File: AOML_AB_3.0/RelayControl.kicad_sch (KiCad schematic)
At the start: 45 parts, among them IC1 CD4043BDR, IC2 CD4043BDR, J5 Conn_01x03, K1 TX2-L2-5V, K10 TX2-L2-5V, K11 TX2-L2-5V, K13 TX2-L2-5V, K2 TX2-L2-5V, K3 TX2-L2-5V, K4 TX2-L2-5V, K5 TX2-L2-5V, K6 TX2-L2-5V, K7 TX2-L2-5V, K8 TX2-L2-5V, K9 TX2-L2-5V, U10 TLP170AM, U11 TLP170AM, U12 TLP170AM, U13 TLP170AM, U14 TLP170AM, U15 TLP170AM, U16 TLP170AM, U17 TLP170AM, U5 ULN2003ADR

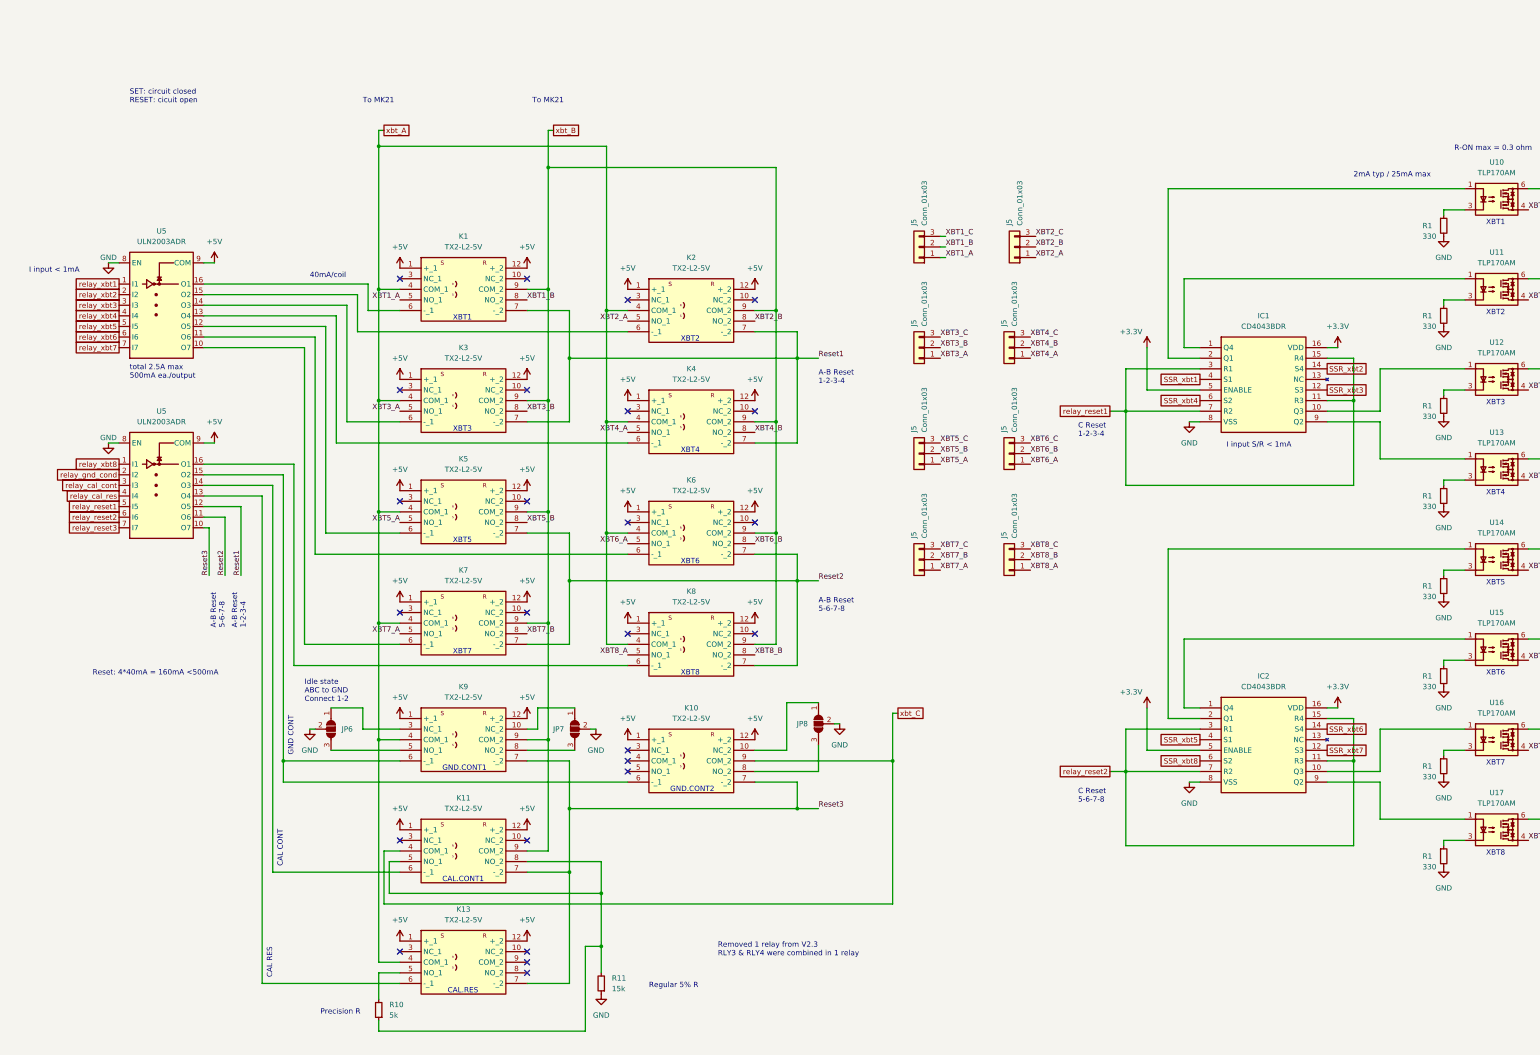
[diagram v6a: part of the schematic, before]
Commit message: Microcontroller pin connections reorganized, test back ground plane routed
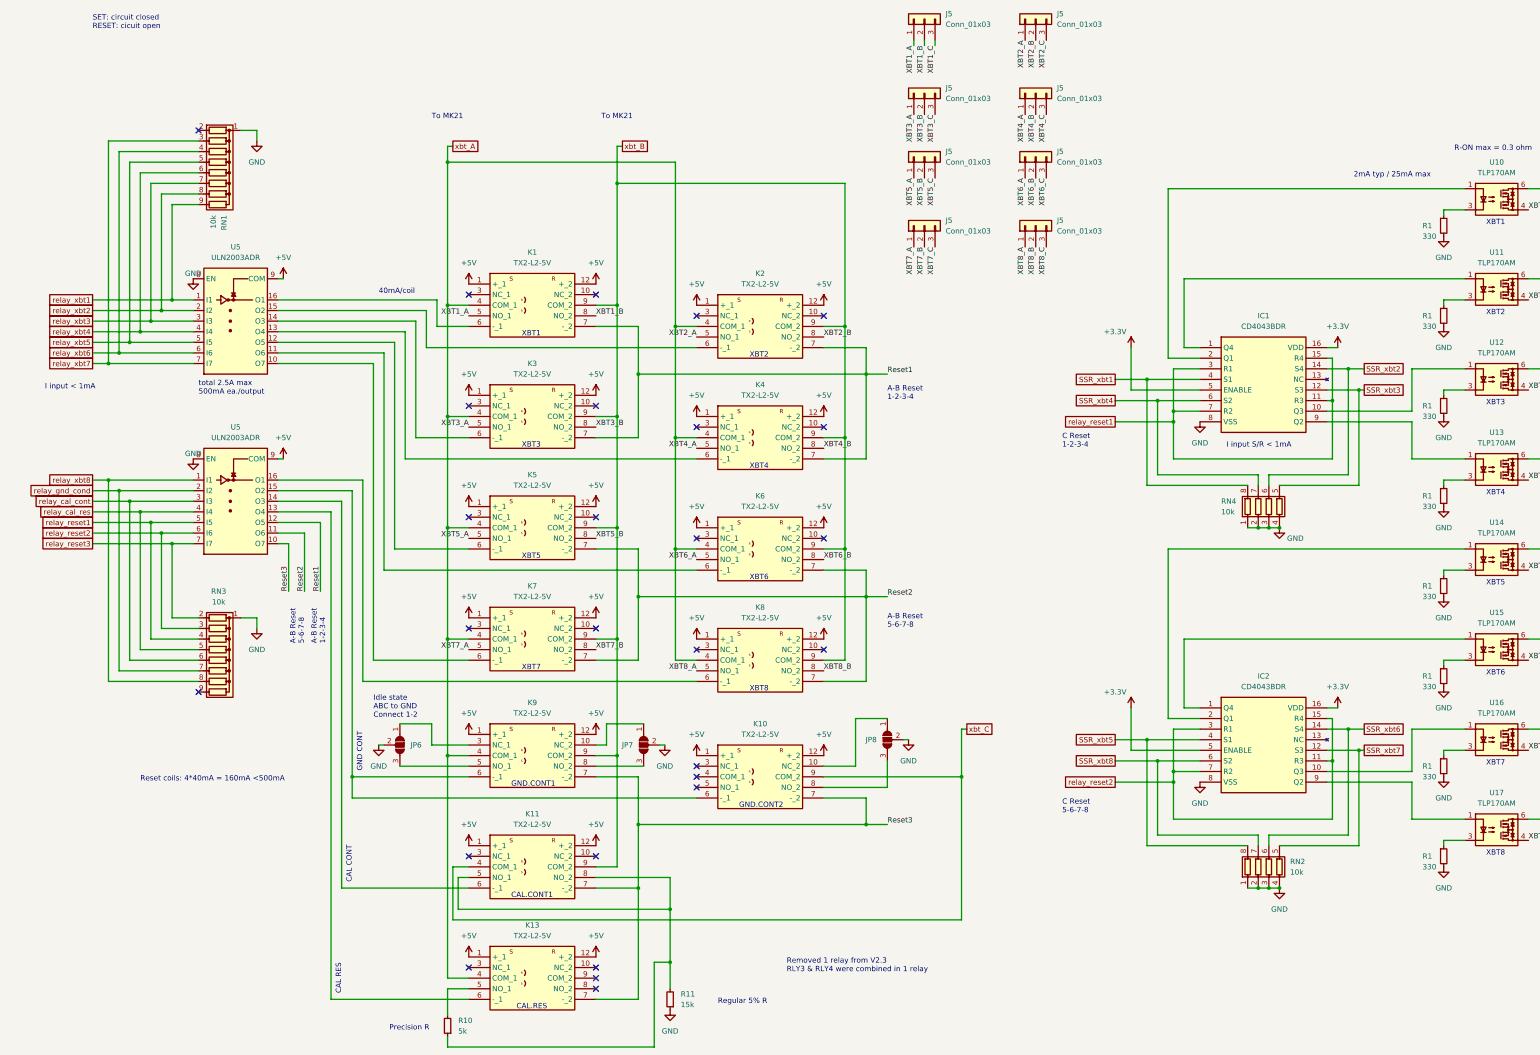
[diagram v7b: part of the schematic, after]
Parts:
- added RN1, RN3: 10k, Resistor_network-10k:SMT_JR-0710KL_YAG, symbol Device:R_Network08
- added RN2, RN4: 10k, Resistor_network_x4_10k-1204:RESCAXS80P320X160X70-8N, symbol Device:R_Pack04
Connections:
- net GND: now also RN1.1 (common), RN2.1 (R1.1), RN2.2 (R2.1), RN2.3 (R3.1), RN2.4 (R4.1), RN3.1 (common), RN4.1 (R1.1), RN4.2 (R2.1), RN4.3 (R3.1), RN4.4 (R4.1)
- net SSR_xbt1: now also RN4.8 (R1.2)
- net SSR_xbt2: now also RN4.6 (R3.2)
- net SSR_xbt3: now also RN4.5 (R4.2)
- net SSR_xbt4: now also RN4.7 (R2.2)
- net SSR_xbt5: now also RN2.8 (R1.2)
- net SSR_xbt6: now also RN2.6 (R3.2)
- net SSR_xbt7: now also RN2.5 (R4.2)
- net SSR_xbt8: now also RN2.7 (R2.2)
- net relay_cal_cont: now also RN3.6 (R5)
- net relay_cal_res: now also RN3.5 (R4)
- net relay_gnd_cond: now also RN3.7 (R6)
- net relay_reset1: now also RN3.4 (R3)
- net relay_reset2: now also RN3.3 (R2)
- net relay_reset3: now also RN3.2 (R1)
- net relay_xbt1: now also RN1.9 (R8)
- net relay_xbt2: now also RN1.8 (R7)
- net relay_xbt3: now also RN1.7 (R6)
- net relay_xbt4: now also RN1.6 (R5)
- net relay_xbt5: now also RN1.5 (R4)
- net relay_xbt6: now also RN1.4 (R3)
- net relay_xbt7: now also RN1.3 (R2)
- net relay_xbt8: now also RN3.8 (R7)
- no-connect marks 25 -> 27
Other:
- note added: "Reset coils: 4*40mA = 160mA <500mA"
- note removed: "Reset: 4*40mA = 160mA <500mA"
- moved on the sheet: J5, JP6, JP7, JP8, K1, K10, K11, K13, K2, K3, K4, K5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

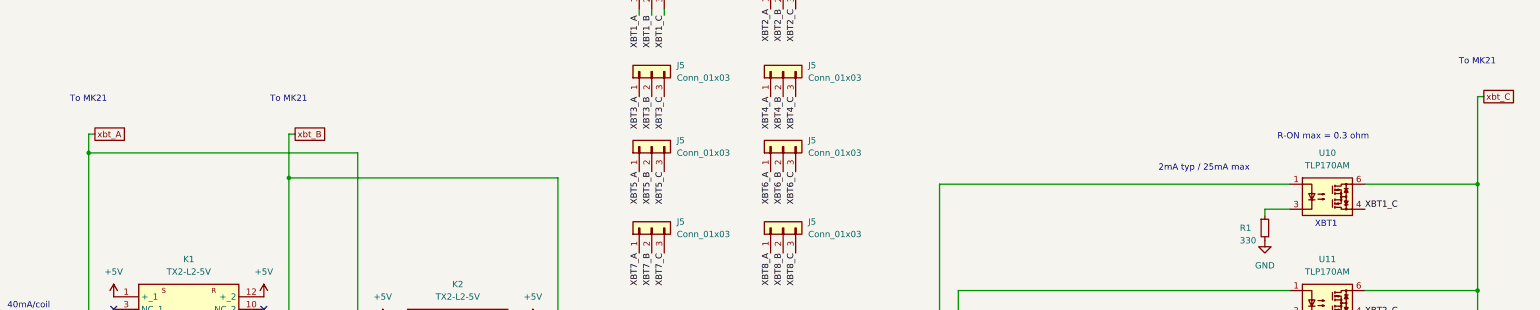
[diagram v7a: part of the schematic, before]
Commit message: test pads added, no tracks yet
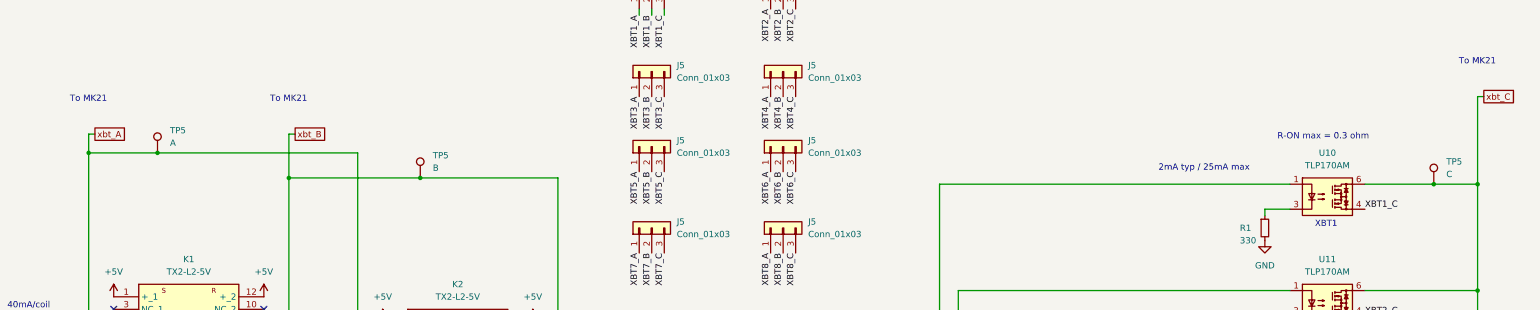
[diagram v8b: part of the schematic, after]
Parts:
- added TP5: B, TestPoint:TestPoint_Pad_1.0x1.0mm, symbol Connector:TestPoint
- added TP5: C, TestPoint:TestPoint_Pad_1.0x1.0mm, symbol Connector:TestPoint
- added TP5: A, TestPoint:TestPoint_Pad_1.0x1.0mm, symbol Connector:TestPoint
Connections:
- net xbt_A: now also TP5.1
- net xbt_B: now also TP5.1
- net xbt_C: now also TP5.1
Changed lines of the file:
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@@
   (junction (at 43.18 91.44) (diameter 0) (color 0 0 0 0)
   )
+  (junction (at 181.61 58.42) (diameter 0) (color 0 0 0 0)
+  )
   (junction (at 33.02 129.54) (diameter 0) (color 0 0 0 0)
   )
@@
   (junction (at 154.94 195.58) (diameter 0) (color 0 0 0 0)
   )
+  (junction (at 387.35 59.69) (diameter 0) (color 0 0 0 0)
+  )
   (junction (at 114.3 53.34) (diameter 0) (color 0 0 0 0)
   )
@@
   (junction (at 114.3 114.3) (diameter 0) (color 0 0 0 0)
   )
+  (junction (at 128.27 53.34) (diameter 0) (color 0 0 0 0)
+  )
   (junction (at 396.24 167.64) (diameter 0) (color 0 0 0 0)
   )
@@
     (stroke (width 0) (type default))
   )
+  (wire (pts (xy 181.61 58.42) (xy 154.94 58.42))
+    (stroke (width 0) (type default))
+  )
   (wire (pts (xy 160.02 119.38) (xy 160.02 104.14))
     (stroke (width 0) (type default))
@@
     (stroke (width 0) (type default))
   )
-  (wire (pts (xy 209.55 58.42) (xy 154.94 58.42))
+  (wire (pts (xy 209.55 58.42) (xy 181.61 58.42))
     (stroke (width 0) (type default))
   )
@@
     (stroke (width 0) (type default))
   )
-  (wire (pts (xy 114.3 53.34) (xy 168.91 53.34))
+  (wire (pts (xy 114.3 53.34) (xy 128.27 53.34))
     (stroke (width 0) (type default))
   )
@@
     (stroke (width 0) (type default))
   )
+  (wire (pts (xy 128.27 53.34) (xy 168.91 53.34))
+    (stroke (width 0) (type default))
+  )
   (wire (pts (xy 353.06 172.72) (xy 358.14 172.72))
     (stroke (width 0) (type default))
@@
     (stroke (width 0) (type default))
   )
+  (wire (pts (xy 387.35 59.69) (xy 396.24 59.69))
+    (stroke (width 0) (type default))
+  )
   (wire (pts (xy 73.66 99.06) (xy 99.06 99.06))
     (stroke (width 0) (type default))
@@
     (stroke (width 0) (type default))
   )
-  (wire (pts (xy 373.38 59.69) (xy 396.24 59.69))
+  (wire (pts (xy 373.38 59.69) (xy 387.35 59.69))
     (stroke (width 0) (type default))
   )
@@
     )
   )
+  (symbol (lib_id "Connector:TestPoint") (at 181.61 58.42 0) (unit 1)
+    (in_bom yes) (on_board yes) (dnp no) (fields_autoplaced)
+    (property "Reference" "TP5" (at 184.15 53.848 0)
+      (effects (font (size 1.27 1.27)) (justify left))
+    )
+    (property "Value" "B" (at 184.15 56.388 0)
+      (effects (font (size 1.27 1.27)) (justify left))
+    )
+    (property "Footprint" "TestPoint:TestPoint_Pad_1.0x1.0mm" (at 186.69 58.42 0)
+      (effects (font (size 1.27 1.27)) hide)
+    )
+    (property "Datasheet" "~" (at 186.69 58.42 0)
+      (effects (font (size 1.27 1.27)) hide)
+    )
+    (pin "1")
+    (instances
+      (project "AOML_AB_3.0"
+        (path "/6a222f58-627e-41ff-951d-9ad8d2e0d7a2"
+          (reference "TP5") (unit 1)
+        )
+        (path "/6a222f58-627e-41ff-951d-9ad8d2e0d7a2/69365a30-fc6f-418a-bc31-d76af2fc83f6"
+          (reference "TP11") (unit 1)
+        )
+      )
+    )
+  )
   (symbol (lib_id "Device:R_Pack04") (at 311.15 222.25 0) (unit 1)
     (in_bom yes) (on_board yes) (dnp no) (fields_autoplaced)
@@
     )
   )
+  (symbol (lib_id "Connector:TestPoint") (at 387.35 59.69 0) (unit 1)
+    (in_bom yes) (on_board yes) (dnp no) (fields_autoplaced)
+    (property "Reference" "TP5" (at 389.89 55.118 0)
+      (effects (font (size 1.27 1.27)) (justify left))
+    )
+    (property "Value" "C" (at 389.89 57.658 0)
+      (effects (font (size 1.27 1.27)) (justify left))
+    )
+    (property "Footprint" "TestPoint:TestPoint_Pad_1.0x1.0mm" (at 392.43 59.69 0)
+      (effects (font (size 1.27 1.27)) hide)
+    )
+    (property "Datasheet" "~" (at 392.43 59.69 0)
+      (effects (font (size 1.27 1.27)) hide)
+    )
+    (pin "1")
+    (instances
+      (project "AOML_AB_3.0"
+        (path "/6a222f58-627e-41ff-951d-9ad8d2e0d7a2"
+          (reference "TP5") (unit 1)
+        )
+        (path "/6a222f58-627e-41ff-951d-9ad8d2e0d7a2/69365a30-fc6f-418a-bc31-d76af2fc83f6"
+          (reference "TP12") (unit 1)
+        )
+      )
+    )
+  )
   (symbol (lib_id "power:+5V") (at 119.38 135.89 0) (unit 1)
     (in_bom yes) (on_board yes) (dnp no) (fields_autoplaced)
@@
         )
       )
+    )
+  )
+  (symbol (lib_id "Connector:TestPoint") (at 128.27 53.34 0) (unit 1)
+    (in_bom yes) (on_board yes) (dnp no) (fields_autoplaced)
+    (property "Reference" "TP5" (at 130.81 48.768 0)
+      (effects (font (size 1.27 1.27)) (justify left))
+    )
+    (property "Value" "A" (at 130.81 51.308 0)
+      (effects (font (size 1.27 1.27)) (justify left))
+    )
+    (property "Footprint" "TestPoint:TestPoint_Pad_1.0x1.0mm" (at 133.35 53.34 0)
+      (effects (font (size 1.27 1.27)) hide)
+    )
+    (property "Datasheet" "~" (at 133.35 53.34 0)
+      (effects (font (size 1.27 1.27)) hide)
+    )
+    (pin "1")
+    (instances
+      (project "AOML_AB_3.0"
+        (path "/6a222f58-627e-41ff-951d-9ad8d2e0d7a2"
+          (reference "TP5") (unit 1)
+        )
+        (path "/6a222f58-627e-41ff-951d-9ad8d2e0d7a2/69365a30-fc6f-418a-bc31-d76af2fc83f6"
+          (reference "TP10") (unit 1)
+        )
+      )
